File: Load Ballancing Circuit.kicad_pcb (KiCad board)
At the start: 2 copper layers, 39.4 x 46.6 mm, 12 parts, among them J1 1757284, U1 LTC4359HMS8#PBF, U2 LTC4359HMS8#PBF

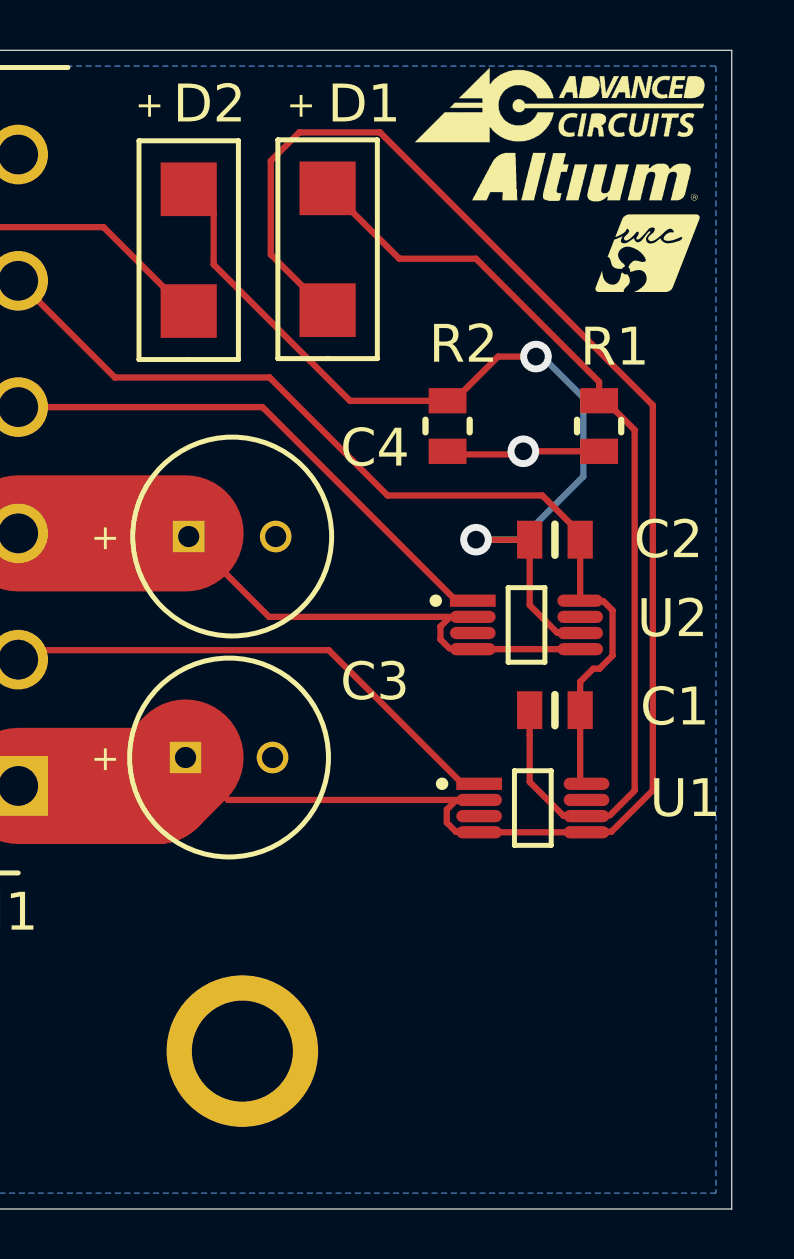
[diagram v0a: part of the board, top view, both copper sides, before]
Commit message: Fix footprint and drc issues
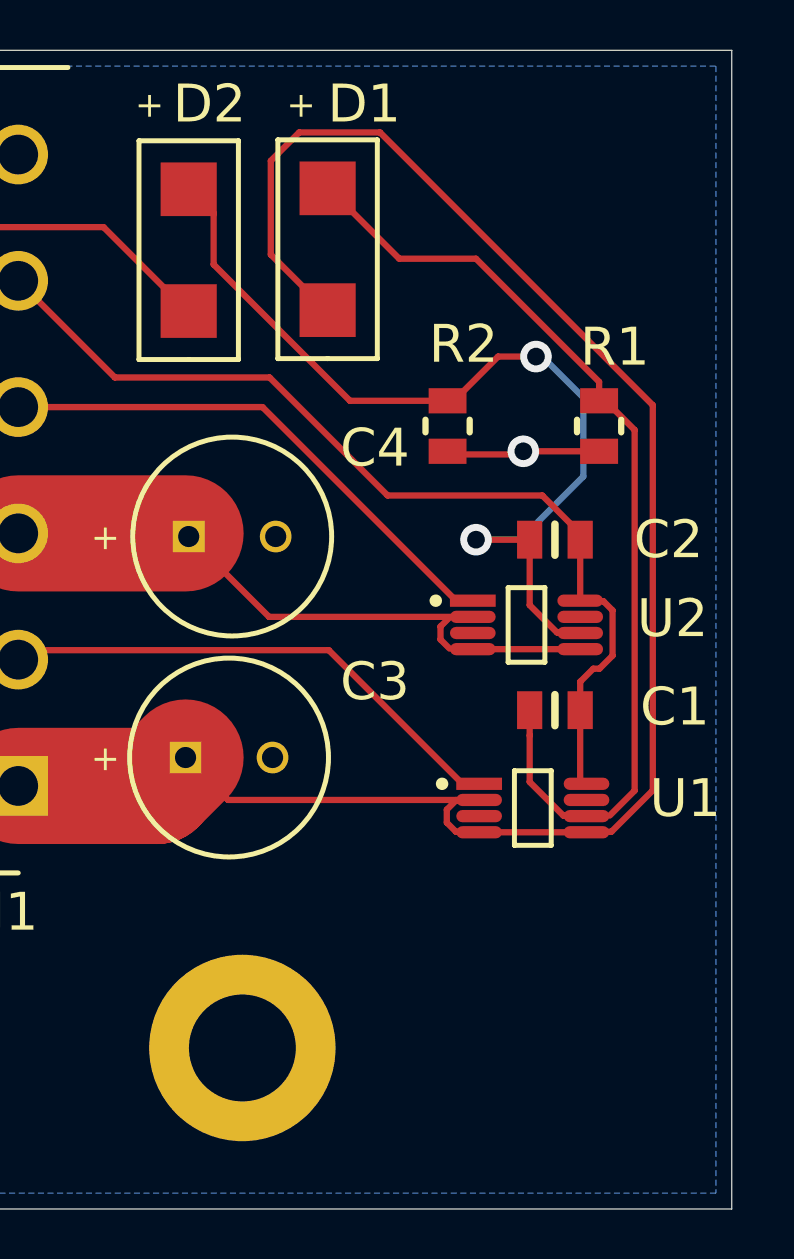
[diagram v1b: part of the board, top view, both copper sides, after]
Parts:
- removed ?: , AltiumImport:
- added REF**: MountingHole_4.3mm_M4_DIN965_Pad, AltiumImport:MountingHole_4.3mm_M4_DIN965_Pad, F.Cu at (148.5, 121.8)
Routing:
- net /V_BAT_IN_2: track 52.2 -> 51.6 mm
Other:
- rule pad_to_mask_clearance: 0 -> 0.05
- board text added: "Load Balancing Board v1.0"

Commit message: added connectors and did layout
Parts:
- removed J1: 1757284, AltiumImport:SHDRRA6W100P0X508_1X6_3240X1200X860P
- removed REF**: MountingHole_4.3mm_M4_DIN965_Pad, AltiumImport:MountingHole_4.3mm_M4_DIN965_Pad
- added C5: 8p, Capacitor_SMD:C_0805_2012Metric_Pad1.18x1.45mm_HandSolder, F.Cu at (164.5, 76.7)
- added C6: 8p, Capacitor_SMD:C_0805_2012Metric_Pad1.18x1.45mm_HandSolder, F.Cu at (164.5, 81.8)
- added J2: 171857-0005, KK254:1718570005, F.Cu at (157.0, 72.0)
- added J3: 171857-0004, KK254:1718570004, F.Cu at (157.0, 85.1)
- added J4: 171857-0006, KK254:1718570006, F.Cu at (157.0, 95.6)
- added R10: 27k, Resistor_SMD:R_0805_2012Metric_Pad1.20x1.40mm_HandSolder, F.Cu at (162.5, 81.8)
- added R3: 10M, Resistor_SMD:R_0805_2012Metric_Pad1.20x1.40mm_HandSolder, F.Cu at (171.4, 86.6)
- added R4: 1.38M, Resistor_SMD:R_0805_2012Metric_Pad1.20x1.40mm_HandSolder, F.Cu at (171.4, 84.7)
- added R5: 10M, Resistor_SMD:R_0805_2012Metric_Pad1.20x1.40mm_HandSolder, F.Cu at (175.1, 86.6)
- added R6: 1.38M, Resistor_SMD:R_0805_2012Metric_Pad1.20x1.40mm_HandSolder, F.Cu at (175.2, 84.7)
- added R7: DNP, Resistor_SMD:R_0805_2012Metric_Pad1.20x1.40mm_HandSolder, F.Cu at (167.7, 86.6)
- added R8: DNP, Resistor_SMD:R_0805_2012Metric_Pad1.20x1.40mm_HandSolder, F.Cu at (167.7, 84.7)
- added R9: 27k, Resistor_SMD:R_0805_2012Metric_Pad1.20x1.40mm_HandSolder, F.Cu at (162.5, 76.7)
- added U3: INA139, Package_TO_SOT_SMD:SOT-23-5, F.Cu at (159.5, 76.7)
- added U4: MAX11615, Package_SO:QSOP-16_3.9x4.9mm_P0.635mm, F.Cu at (171.9, 79.2)
- added U5: INA139, Package_TO_SOT_SMD:SOT-23-5, F.Cu at (159.5, 81.8)
- moved D2 27.9 mm to (171.3, 102.2), turned to 0 degrees
- moved C3 24.7 mm to (162.2, 91.3), turned to -90 degrees
- moved R2 23.6 mm to (178.4, 106.3), turned to 180 degrees
- moved U1 20.2 mm to (171.3, 95.2)
- moved C1 19.8 mm to (176.1, 95.3), turned to 0 degrees
- moved D1 19.4 mm to (171.3, 91.2), turned to 0 degrees
- moved C2 15.9 mm to (176.2, 106.3), turned to 0 degrees
- moved C4 15.8 mm to (162.1, 102.5), turned to -90 degrees
- moved R1 15.5 mm to (178.3, 95.3), turned to 180 degrees
- moved U2 11.5 mm to (171.4, 106.2)
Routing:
- net 3V3: track 0.00 -> 49.8 mm, vias 0 -> 4
- net /V_BAT_IN_1: track 73.7 -> 33.1 mm
- net /I2C_SCL: track 0.00 -> 26.0 mm
- net /I2C_SDA: track 0.00 -> 25.9 mm
- net Net-(D1-2): track 38.5 -> 12.7 mm
- net Net-(D2-2): track 38.0 -> 12.8 mm, vias 2 -> 0
- net Net-(U4-AIN2): track 0.00 -> 15.8 mm
- net Net-(U4-AIN0): track 0.00 -> 10.0 mm
- net Net-(U4-AIN6): track 0.00 -> 7.68 mm
- net /GATE_2: track 21.5 -> 14.4 mm, vias 0 -> 1
- net Net-(U4-AIN4): track 0.00 -> 6.07 mm
- net /SNS2+: track 0.00 -> 5.52 mm
- net /SNS1+: track 0.00 -> 5.51 mm
- net GND: track 5.21 -> 0.00 mm, vias 1 -> 0
- net /GATE_1: track 20.9 -> 16.8 mm, vias 0 -> 1
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- added copper zone on F.Cu, net GND
- removed copper zone on B.Cu, net (none)
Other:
- board size 39.4 x 46.6 mm -> 32.6 x 38.4 mm
- board text removed: "+"
- board text removed: "Load Balancing Board v1.0"

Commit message: board is now now a weird size
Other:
- board size 32.6 x 38.4 mm -> 33 x 39 mm
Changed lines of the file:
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@@
       (net 17 "/I2C_SCL") (pinfunction "4") (pintype "passive"))
   )
-  (gr_rect (start 149.9511 72.2331) (end 182.5511 110.6331)
+  (gr_rect (start 149.8511 71.9331) (end 182.8511 110.9331)
     (stroke (width 0.1016) (type default)) (fill none) (layer "Edge.Cuts"))
+  (dimension (type aligned) (layer "Edge.Cuts")
+    (pts (xy 182.8511 71.9331) (xy 149.8511 71.9331))
+    (height 5.5669)
+    (gr_text "33.0000 mm" (at 166.3511 65.2162) (layer "Edge.Cuts")
+      (effects (font (size 1 1) (thickness 0.15)))
+    )
+    (format (prefix "") (suffix "") (units 2) (units_format 1) (precision 4))
+    (style (thickness 0.1016) (arrow_length 1.27) (text_position_mode 0) (extension_height 0.58642) (extension_offset 0.508) keep_text_aligned)
+  )
+  (dimension (type aligned) (layer "Edge.Cuts")
+    (pts (xy 182.8511 110.9331) (xy 182.8511 71.9331))
+    (height 10.1)
+    (gr_text "39.0000 mm" (at 191.8011 91.4331 90) (layer "Edge.Cuts")
+      (effects (font (size 1 1) (thickness 0.15)))
+    )
+    (format (prefix "") (suffix "") (units 2) (units_format 1) (precision 4))
+    (style (thickness 0.1016) (arrow_length 1.27) (text_position_mode 0) (extension_height 0.58642) (extension_offset 0.508) keep_text_aligned)
+  )
   (segment (start 173.5511 105.21795) (end 173.51095 105.2581) (width 0.127) (layer "F.Cu") (net 1))
   (segment (start 173.51095 105.2581) (end 173.56995 105.3171) (width 0.127) (layer "F.Cu") (net 1))

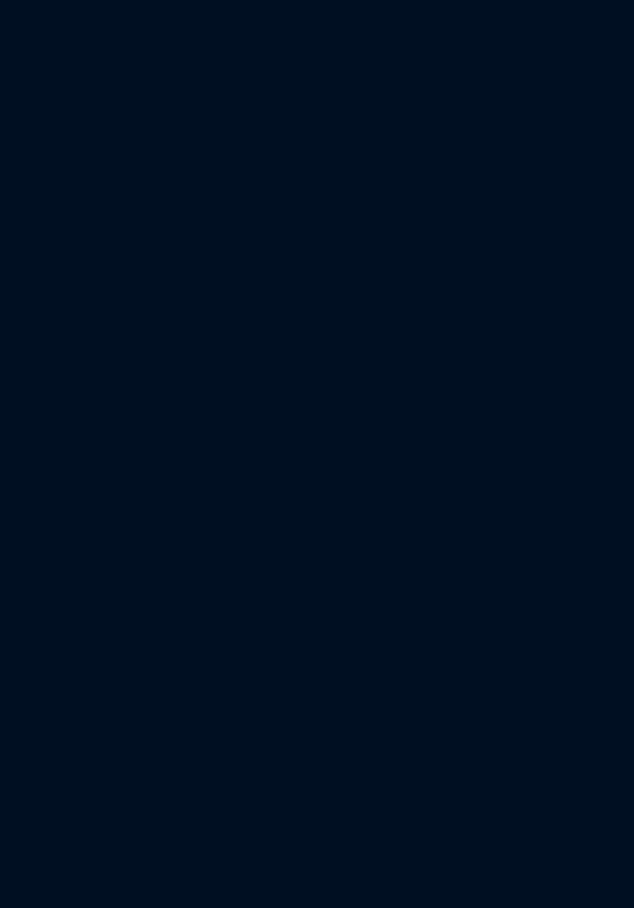
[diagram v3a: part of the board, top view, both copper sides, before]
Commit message: added rc lp and cm filter to vdiv
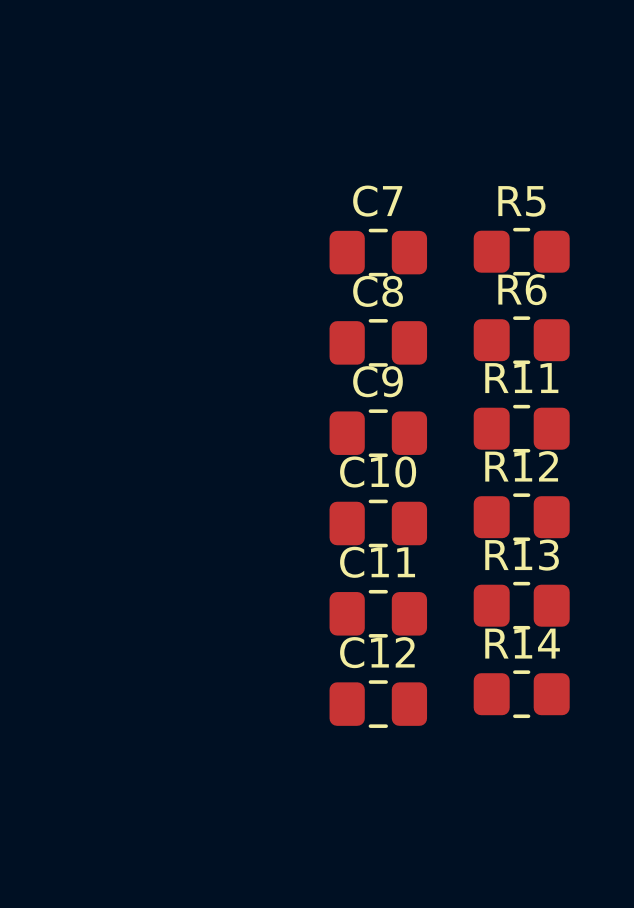
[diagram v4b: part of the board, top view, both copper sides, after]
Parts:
- added C10: 10uF, Capacitor_SMD:C_0805_2012Metric_Pad1.18x1.45mm_HandSolder, F.Cu at (202.4, 83.9)
- added C11: 10uF, Capacitor_SMD:C_0805_2012Metric_Pad1.18x1.45mm_HandSolder, F.Cu at (202.4, 86.9)
- added C12: 10uF, Capacitor_SMD:C_0805_2012Metric_Pad1.18x1.45mm_HandSolder, F.Cu at (202.4, 89.9)
- added C7: 10uF, Capacitor_SMD:C_0805_2012Metric_Pad1.18x1.45mm_HandSolder, F.Cu at (202.4, 74.9)
- added C8: 10uF, Capacitor_SMD:C_0805_2012Metric_Pad1.18x1.45mm_HandSolder, F.Cu at (202.4, 77.9)
- added C9: 10uF, Capacitor_SMD:C_0805_2012Metric_Pad1.18x1.45mm_HandSolder, F.Cu at (202.4, 80.9)
- added R11: 1k, Resistor_SMD:R_0805_2012Metric_Pad1.20x1.40mm_HandSolder, F.Cu at (207.2, 80.7)
- added R12: 1k, Resistor_SMD:R_0805_2012Metric_Pad1.20x1.40mm_HandSolder, F.Cu at (207.2, 83.7)
- added R13: 1k, Resistor_SMD:R_0805_2012Metric_Pad1.20x1.40mm_HandSolder, F.Cu at (207.2, 86.6)
- added R14: 1k, Resistor_SMD:R_0805_2012Metric_Pad1.20x1.40mm_HandSolder, F.Cu at (207.2, 89.6)
- added R5: 10M, Resistor_SMD:R_0805_2012Metric_Pad1.20x1.40mm_HandSolder, F.Cu at (207.2, 74.8)
- added R6: 1.38M, Resistor_SMD:R_0805_2012Metric_Pad1.20x1.40mm_HandSolder, F.Cu at (207.2, 77.8)
- C5, C6: value 8p -> 350p
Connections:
- R3 pad 1: Net-(U4-AIN4) -> Net-(R11-Pad2)
- R4 pad 1: Net-(U4-AIN4) -> Net-(R11-Pad2)
- U4 pad 10: GND -> Net-(U4-AIN5)
- U4 pad 12: GND -> Net-(U4-AIN7)

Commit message: changed circuit
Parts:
- removed C11, C12, C7, C8: 10uF, Capacitor_SMD:C_0805_2012Metric_Pad1.18x1.45mm_HandSolder
- removed R12, R13: 1k, Resistor_SMD:R_0805_2012Metric_Pad1.20x1.40mm_HandSolder
- removed the R5 at (175.1, 86.6)
- removed the R5 at (207.2, 74.8)
- removed the R6 at (207.2, 77.8)
- removed the R6 at (175.2, 84.7)
- added R5: 10M, Resistor_SMD:R_0805_2012Metric_Pad1.20x1.40mm_HandSolder, F.Cu at (175.1, 86.6)
- added R6: 1.38M, Resistor_SMD:R_0805_2012Metric_Pad1.20x1.40mm_HandSolder, F.Cu at (175.1, 84.7)
- moved R14 32.2 mm to (178.0, 76.1)
- moved R11 29.3 mm to (178.0, 82.1)
- moved C10 25.1 mm to (178.0, 78.1), turned to 180 degrees
- moved C9 24.5 mm to (178.0, 80.1), turned to 180 degrees
- moved J4 0.90 mm to (157.0, 94.7)
- moved J3 0.60 mm to (157.0, 84.5)
- moved J2 0.21 mm to (157.0, 71.8)
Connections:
- U4 pad 10: Net-(U4-AIN5) -> GND
- U4 pad 12: Net-(U4-AIN7) -> GND
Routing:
- net Net-(R14-Pad2): track 0.00 -> 15.4 mm
- net Net-(R11-Pad2): track 0.00 -> 9.58 mm
- net /V_BAT_OUT: track 37.6 -> 40.6 mm
- net Net-(U4-AIN6): track 7.68 -> 5.55 mm
- net 3V3: track 49.8 -> 47.7 mm
- net Net-(D2-2): track 12.8 -> 11.0 mm
- net Net-(D1-2): track 12.7 -> 11.0 mm
- net /GATE_1: track 16.8 -> 15.3 mm, vias 1 -> 0
- net Net-(U4-AIN4): track 6.07 -> 4.74 mm
- net /I2C_SDA: track 25.9 -> 25.1 mm
- net /I2C_SCL: track 26.0 -> 26.7 mm
- net /GATE_2: track 14.4 -> 14.2 mm, vias 1 -> 0
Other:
- board size 33 x 39 mm -> 33 x 38.3 mm
